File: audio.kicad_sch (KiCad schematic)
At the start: 15 parts, among them J6 Audio Left, J7 Stereo, J8 Audio Right, U14 74LS08

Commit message: Progress routing
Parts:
- JP6: value Jumper_3_Open -> Mono_Mix

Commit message: Revise layout and tracing
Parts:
- removed J7: Stereo, Connector_PinHeader_2.54mm:PinHeader_1x03_P2.54mm_Vertical, symbol Connector:Conn_01x03_Pin
- removed JP6: Mono_Mix, Connector_PinHeader_2.54mm:PinHeader_1x03_P2.54mm_Vertical, symbol Jumper:Jumper_3_Open
- added JP6: Jumper_2_Small_Bridged, Jumper:SolderJumper-2_P1.3mm_Bridged_Pad1.0x1.5mm, symbol Jumper:Jumper_2_Small_Bridged
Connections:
- net OUT_L: now also JP6.1 (A)
- new net SOUND: JP6.2 (B)

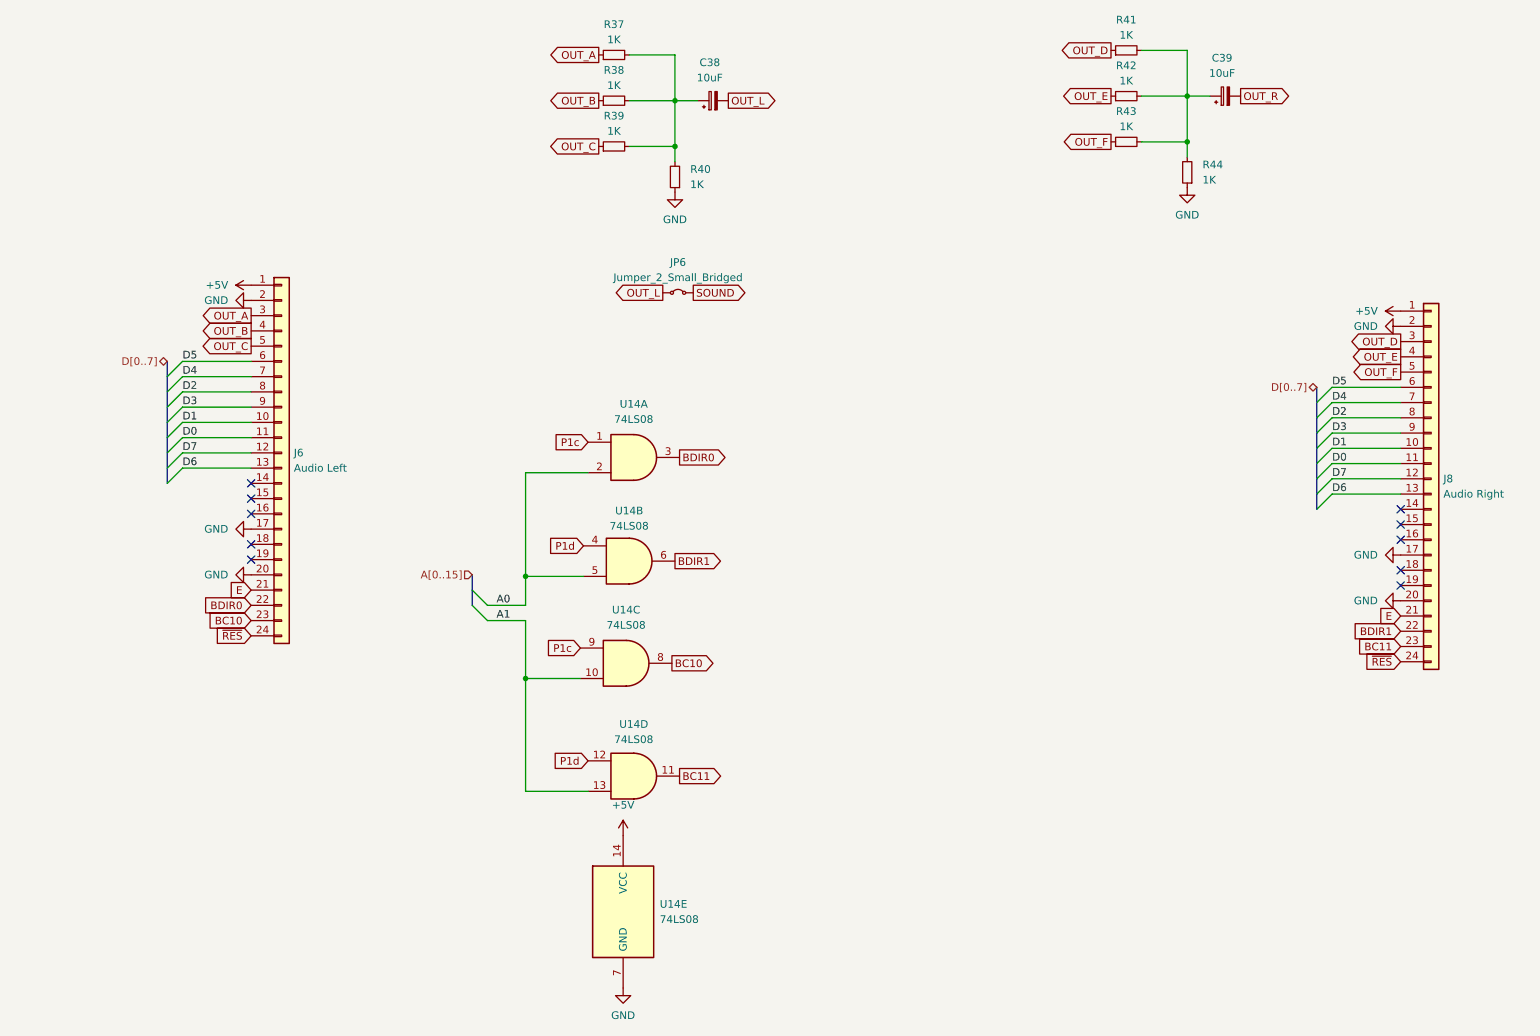
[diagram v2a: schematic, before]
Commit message: add isa style slots
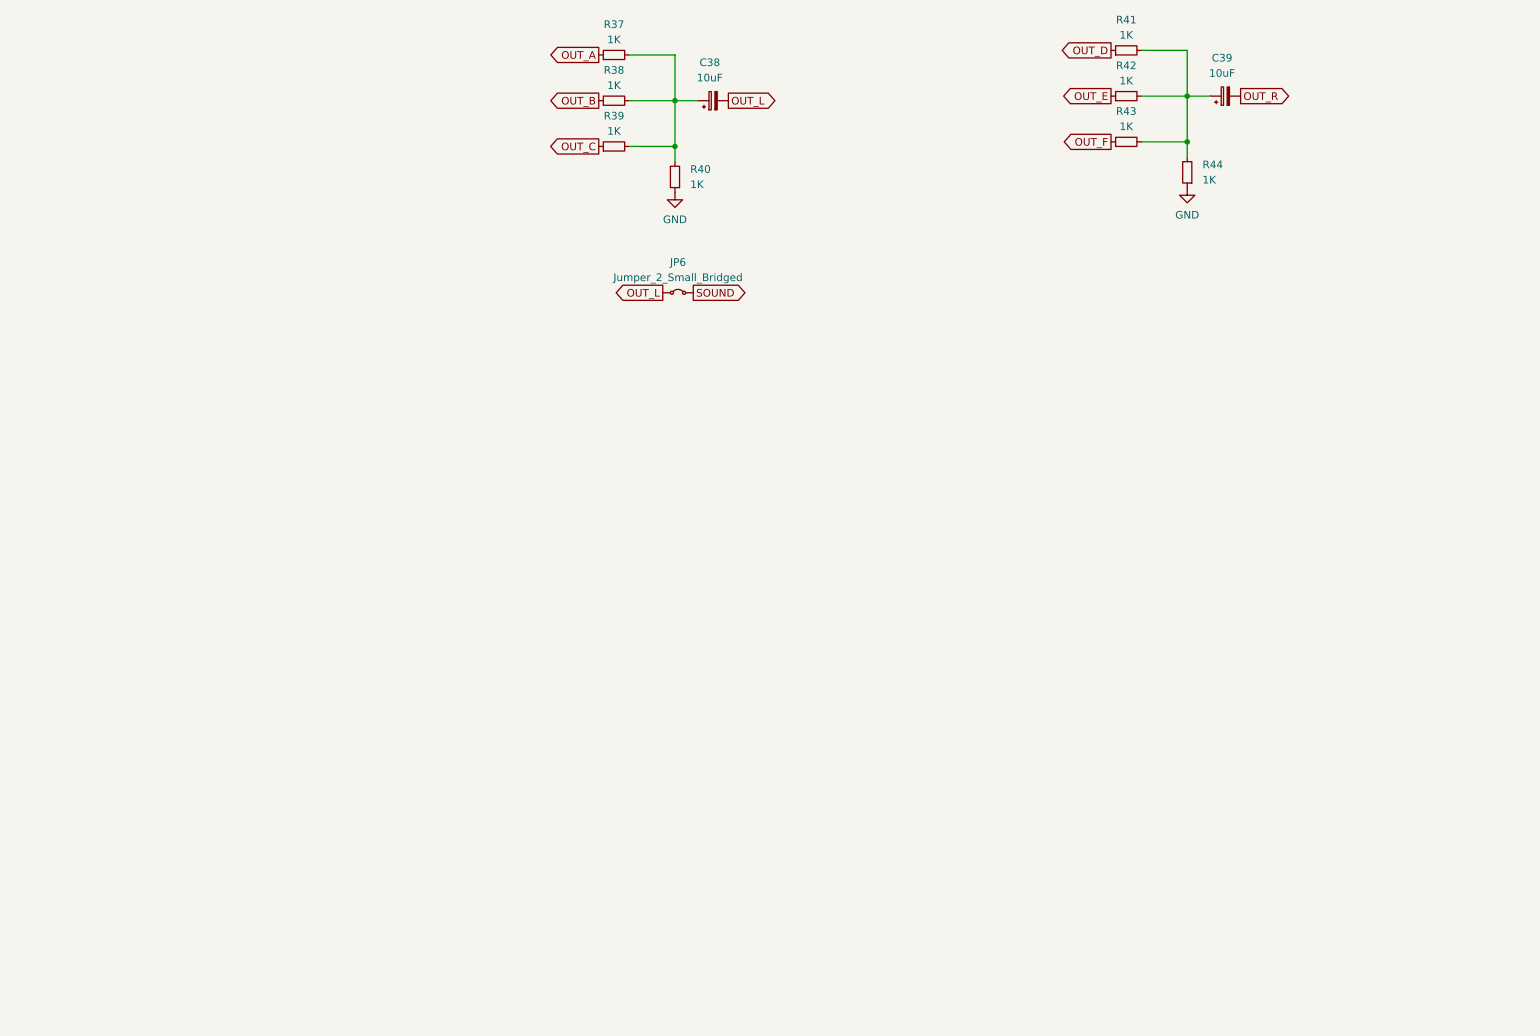
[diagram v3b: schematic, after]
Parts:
- removed J6: Audio Left, Dragon:AY-QTHT, symbol Connector_Generic:Conn_01x24
- removed J8: Audio Right, Dragon:AY-QTHT, symbol Connector_Generic:Conn_01x24
- removed U14: 74LS08, Package_SO:SO-14_3.9x8.65mm_P1.27mm, symbol 74xx:74LS08
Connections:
- no-connect marks 10 -> 0

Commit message: add data bus transceiver
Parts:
- R37, R38, R39, R40, R41, R42, R43, R44: DigiKey (none) -> RNCP0805FTD1K00CT-ND
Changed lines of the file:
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@@
+			)
+		)
+		(property "DigiKey" "RNCP0805FTD1K00CT-ND"
+			(at 197.866 26.924 90)
+			(effects
+				(font
+					(size 1.27 1.27)
+				)
+				(hide yes)
 			)
 		)
@@
 			)
 		)
+		(property "DigiKey" "RNCP0805FTD1K00CT-ND"
+			(at 112.522 27.686 90)
+			(effects
+				(font
+					(size 1.27 1.27)
+				)
+				(hide yes)
+			)
+		)
 		(pin "1"
 		)
@@
 			)
 		)
+		(property "DigiKey" "RNCP0805FTD1K00CT-ND"
+			(at 112.522 42.926 90)
+			(effects
+				(font
+					(size 1.27 1.27)
+				)
+				(hide yes)
+			)
+		)
 		(pin "1"
 		)
@@
 			)
 		)
+		(property "DigiKey" "RNCP0805FTD1K00CT-ND"
+			(at 197.866 42.164 90)
+			(effects
+				(font
+					(size 1.27 1.27)
+				)
+				(hide yes)
+			)
+		)
 		(pin "1"
 		)
@@
 			)
 		)
+		(property "DigiKey" "RNCP0805FTD1K00CT-ND"
+			(at 112.522 35.306 90)
+			(effects
+				(font
+					(size 1.27 1.27)
+				)
+				(hide yes)
+			)
+		)
 		(pin "1"
 		)
@@
 			)
 		)
+		(property "DigiKey" "RNCP0805FTD1K00CT-ND"
+			(at 122.682 48.006 0)
+			(effects
+				(font
+					(size 1.27 1.27)
+				)
+				(hide yes)
+			)
+		)
 		(pin "1"
 		)
@@
 			)
 		)
+		(property "DigiKey" "RNCP0805FTD1K00CT-ND"
+			(at 197.866 34.544 90)
+			(effects
+				(font
+					(size 1.27 1.27)
+				)
+				(hide yes)
+			)
+		)
 		(pin "1"
 		)
@@
 			(at 208.026 47.244 0)
 			(effects
+				(font
+					(size 1.27 1.27)
+				)
+				(hide yes)
+			)
+		)
+		(property "DigiKey" "RNCP0805FTD1K00CT-ND"
+			(at 208.026 47.244 0)
+			(effects
